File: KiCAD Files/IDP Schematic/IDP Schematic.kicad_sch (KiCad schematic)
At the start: 28 parts

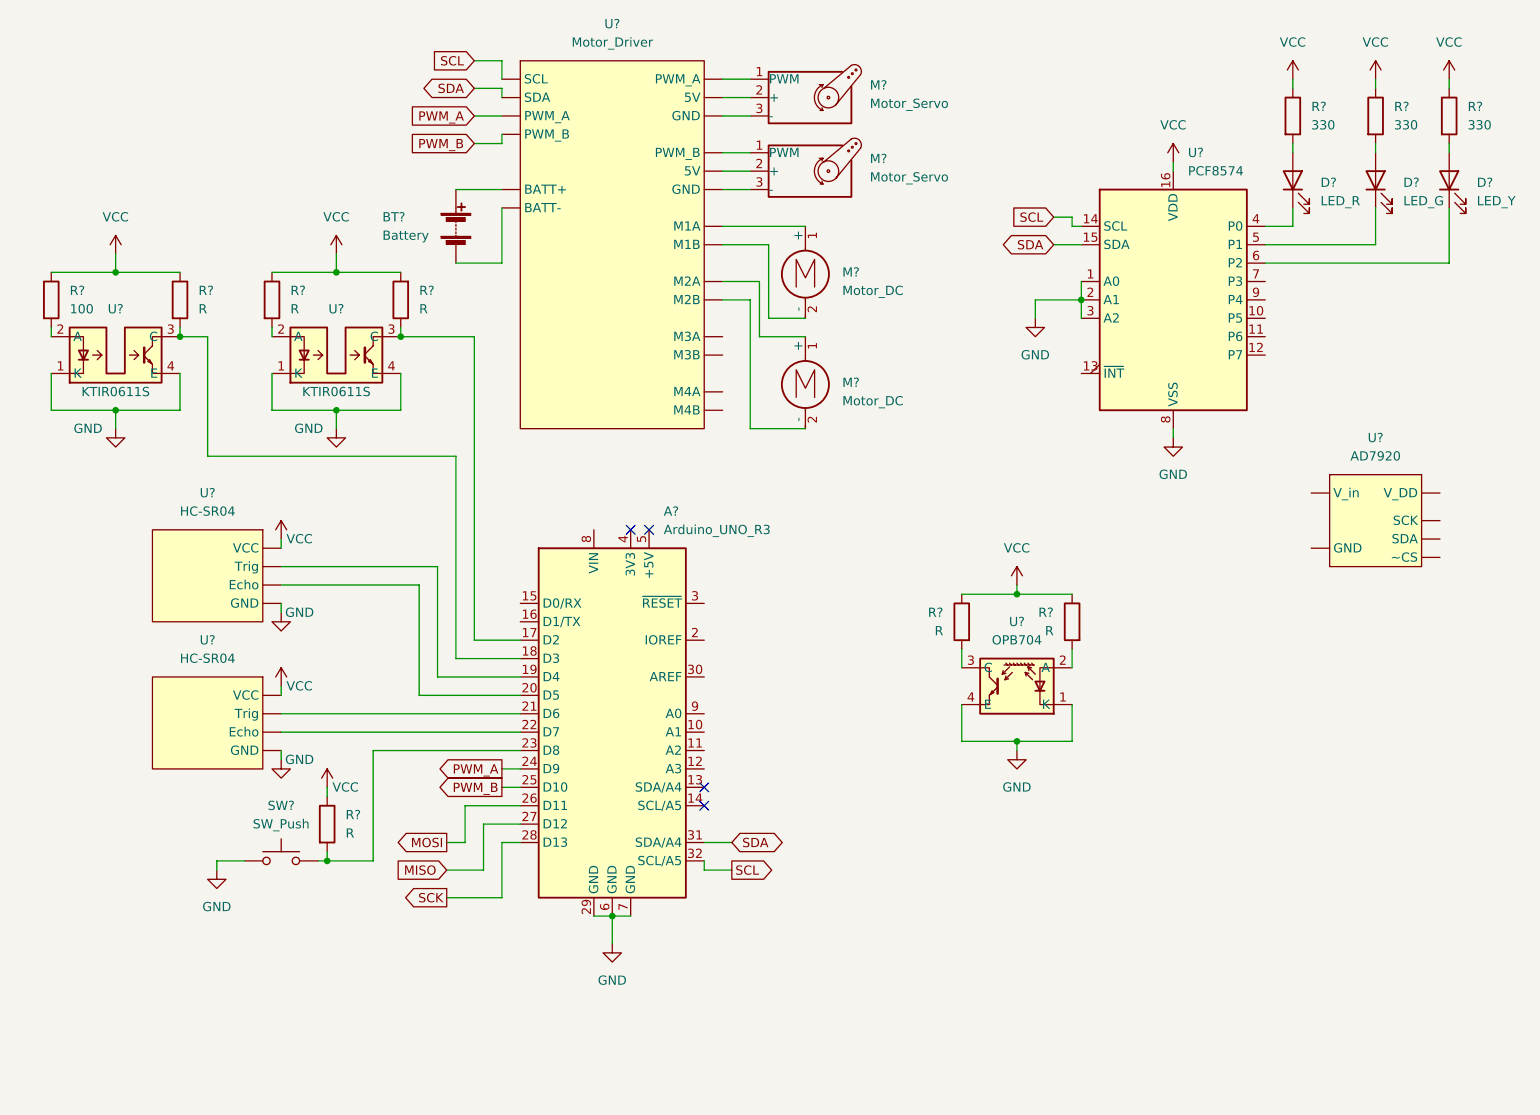
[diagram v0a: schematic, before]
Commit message: simplified kicad schematic
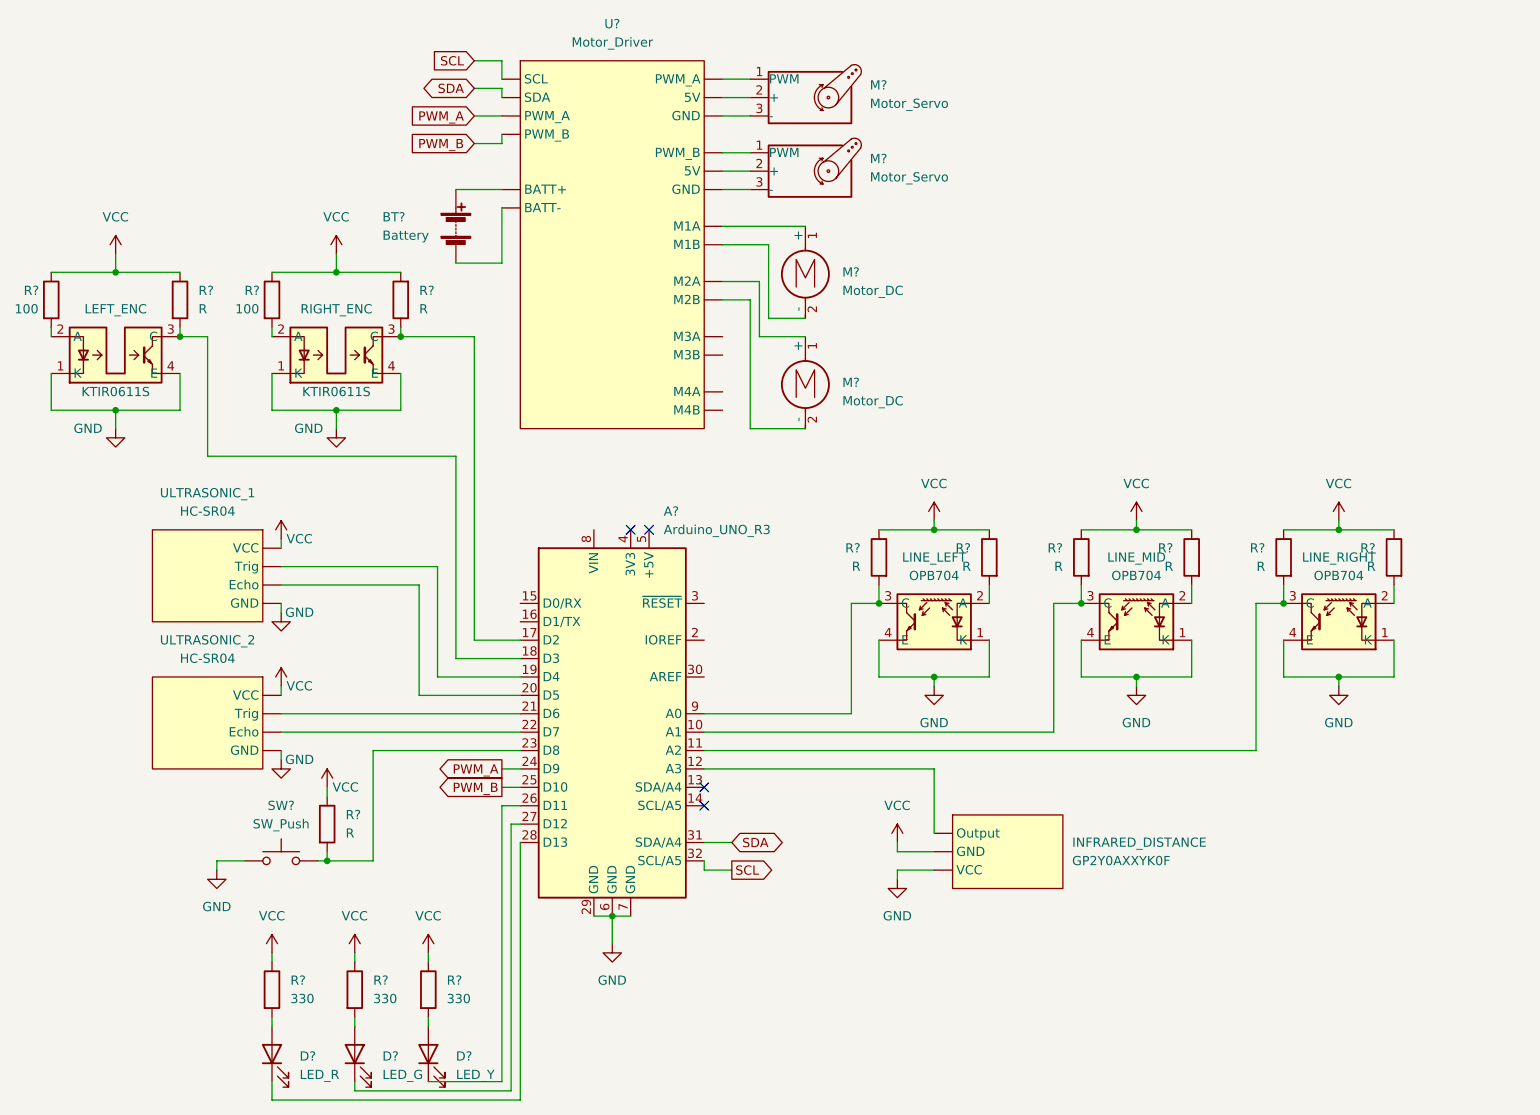
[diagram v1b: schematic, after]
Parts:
- removed D?: LED_R, symbol Device:LED
- removed D?: LED_Y, symbol Device:LED
- removed D?: LED_G, symbol Device:LED
- removed R? (x3): 330, symbol Device:R
- removed U?: AD7920, symbol IEP:AD7920
- removed U?: PCF8574, symbol Interface_Expansion:PCF8574
- added D?: LED_Y, symbol Device:LED
- added D?: LED_G, symbol Device:LED
- added D?: LED_R, symbol Device:LED
- added INFRARED_DISTANCE: GP2Y0AXXYK0F, symbol Integrated_Design_Project:GP2Y0AXXYK0F
- added LINE_MID, LINE_RIGHT: OPB704, symbol Integrated_Design_Project:OPB704
- added R? (x3): 330, symbol Device:R
- added R? (x4): R, symbol Device:R
- R?: value R -> 100
- gave numbers to parts that had none: 5
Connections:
- net GND: now also INFRARED_DISTANCE. (VCC), LINE_MID.1 (K), LINE_MID.4 (E), LINE_RIGHT.1 (K), LINE_RIGHT.4 (E)
- net VCC: now also INFRARED_DISTANCE. (VCC), R?.1, R?.1, R?.1, R?.1, R?.1, R?.1, R?.1
- net at A?.10 (A1): now also LINE_MID.3 (C), R?.2
- net at A?.11 (A2): now also LINE_RIGHT.3 (C), R?.2
- net at A?.12 (A3): now also INFRARED_DISTANCE. (VCC)
- net at A?.9 (A0): now also LINE_LEFT.3 (C), R?.2
- net MISO: no longer names the net of A?.27 (D12)
- net MISO: now also D?.1 (K)
- net MOSI: no longer names the net of A?.26 (D11)
- net MOSI: now also D?.1 (K)
- net SCK: no longer names the net of A?.28 (D13)
- net SCK: now also D?.1 (K)
- new net: D?.2 (A), R?.2 (x3)
- new net: LINE_RIGHT.2 (A), R?.2
- new net: LINE_MID.2 (A), R?.2
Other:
- moved on the sheet: LINE_LEFT, R?

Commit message: added mon arduino final
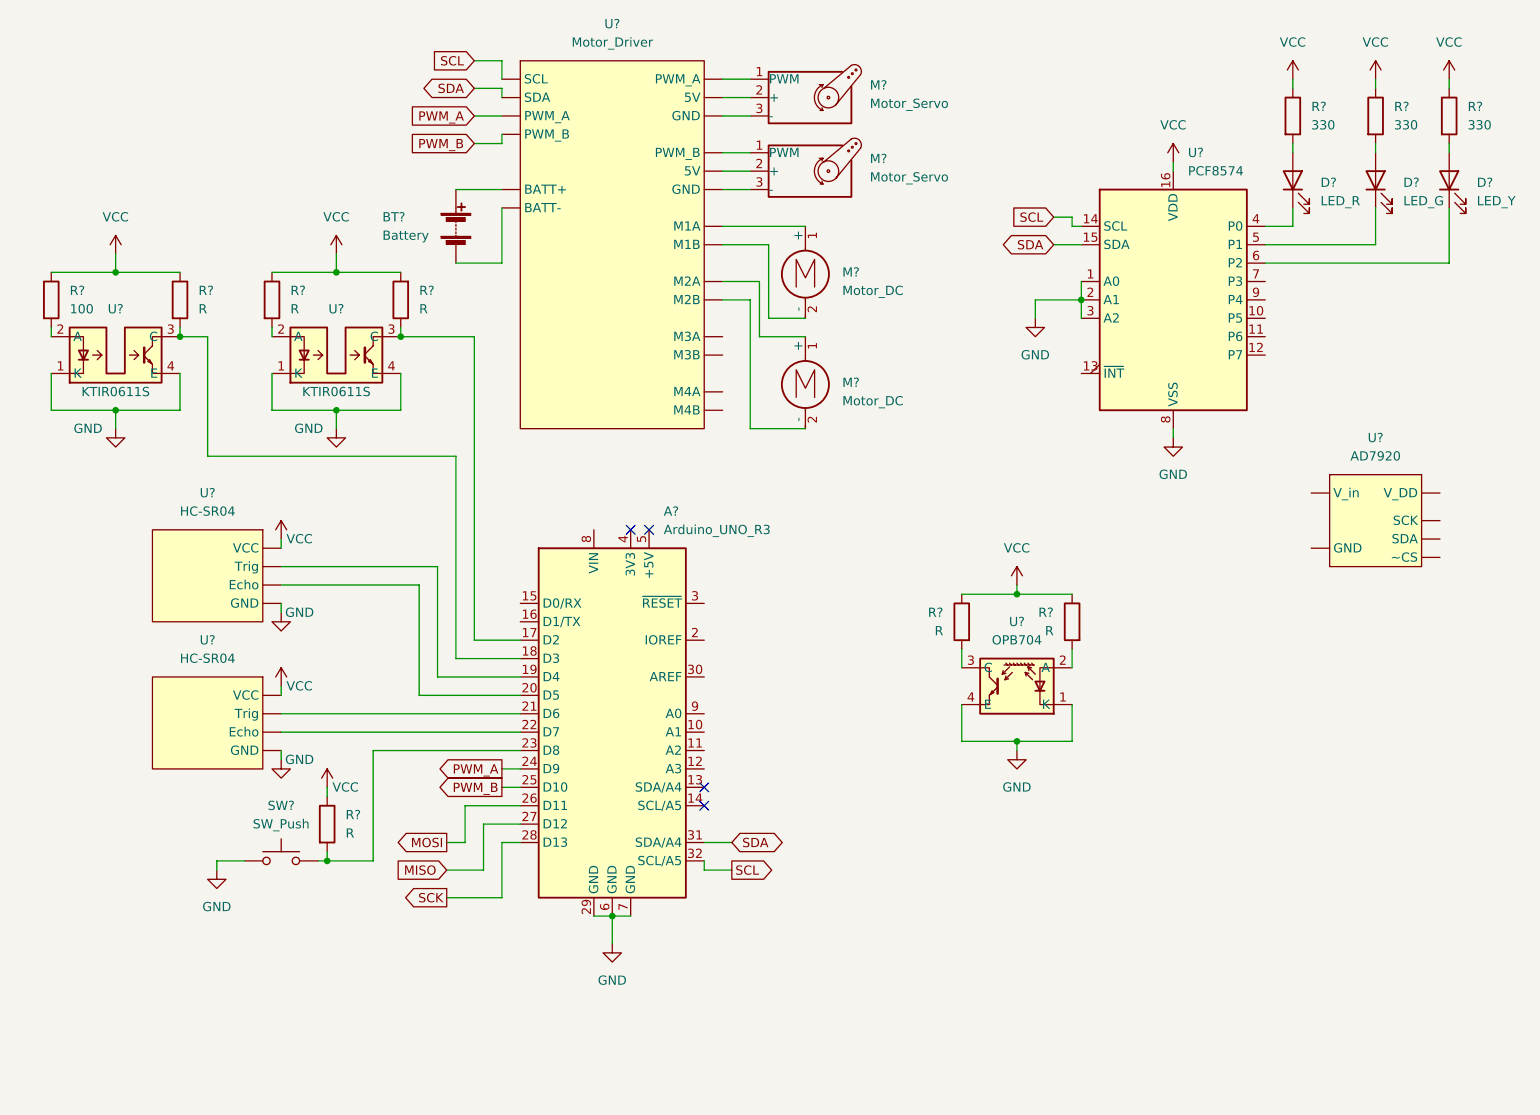
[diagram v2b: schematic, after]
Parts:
- removed D?: LED_Y, symbol Device:LED
- removed D?: LED_G, symbol Device:LED
- removed D?: LED_R, symbol Device:LED
- removed INFRARED_DISTANCE: GP2Y0AXXYK0F, symbol Integrated_Design_Project:GP2Y0AXXYK0F
- removed LINE_MID, LINE_RIGHT: OPB704, symbol Integrated_Design_Project:OPB704
- removed R? (x3): 330, symbol Device:R
- removed R? (x4): R, symbol Device:R
- added D?: LED_R, symbol Device:LED
- added D?: LED_Y, symbol Device:LED
- added D?: LED_G, symbol Device:LED
- added R? (x3): 330, symbol Device:R
- added U?: AD7920, symbol IEP:AD7920
- added U?: PCF8574, symbol Interface_Expansion:PCF8574
- R?: value 100 -> R
- renumbered LEFT_ENC to U?, RIGHT_ENC to U?, ULTRASONIC_2 to U?, ULTRASONIC_1 to U?, LINE_LEFT to U?
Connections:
- net GND: now also U?.1 (A0), U?.2 (A1), U?.3 (A2), U?.8 (VSS)
- net SCL: now also U?.14 (SCL)
- net SDA: now also U?.15 (SDA)
- net VCC: now also R?.1, R?.1, R?.1, U?.16 (VDD)
- net MOSI: now reaches A?.26 (D11)
- net MISO: now reaches A?.27 (D12)
- net SCK: now reaches A?.28 (D13)
- net at R?.2, U?.3 (C): no longer A?.9 (A0)
- new net: D?.1 (K), U?.4 (P0)
- new net: D?.2 (A), R?.2 (x3)
- new net: D?.1 (K), U?.6 (P2)
- new net: D?.1 (K), U?.5 (P1)
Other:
- moved on the sheet: R?, U?
